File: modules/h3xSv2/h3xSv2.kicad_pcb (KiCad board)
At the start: 2 copper layers, 135.9 x 40.6 mm, 25 parts, among them J1 Conn_01x10_Male, J10 Conn_01x02_Male, J11 Conn_01x06_Male, J12 Conn_01x10_Male, J13 Conn_01x10_Male, J2 Conn_01x10_Male, J3 Conn_01x10_Male, J4 Conn_01x10_Male, J5 Conn_01x04_Male, J6 Conn_01x04_Male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

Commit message: New h3xSv2 is ready
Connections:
- J7 pad 12: VCC -> /13
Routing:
- net /A5: track 106.8 -> 161.7 mm, vias 1 -> 3
- net /3: track 102.6 -> 157.2 mm, vias 1 -> 3
- net /2: track 106.4 -> 160.7 mm, vias 1 -> 3
- net /A4: track 108.7 -> 162.7 mm, vias 1 -> 3
- net /4: track 97.5 -> 151.1 mm, vias 1 -> 3
- net /A3: track 65.9 -> 118.9 mm, vias 1 -> 3
- net /5: track 92.8 -> 145.5 mm, vias 1 -> 3
- net /A2: track 64.0 -> 116.0 mm, vias 1 -> 3
- net /6: track 88.2 -> 140.0 mm, vias 1 -> 3
- net /7: track 84.0 -> 134.8 mm, vias 1 -> 3
- net /A1: track 61.9 -> 112.6 mm, vias 1 -> 3
- net GND: track 168.3 -> 218.9 mm, vias 2 -> 4
- net /A0: track 60.2 -> 110.3 mm, vias 1 -> 3
- net /8: track 79.7 -> 129.6 mm, vias 1 -> 3
- net /13: track 75.1 -> 124.3 mm, vias 1 -> 3
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
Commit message: Add hash & gerber
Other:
- rule solder_mask_min_width: 0.25 -> 0.1
- board text added: "11.11.2020"
- board text added: "3f4a18"
- board text added: "v2"

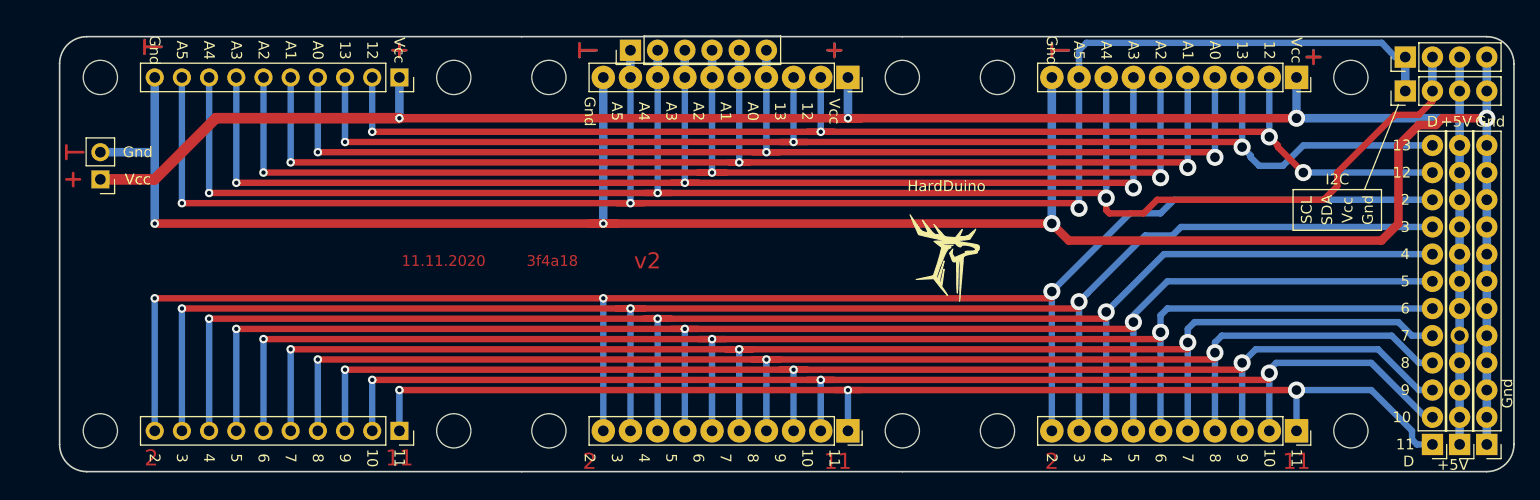
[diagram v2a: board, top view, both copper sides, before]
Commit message: Now 2x shields have distance between 1x parts
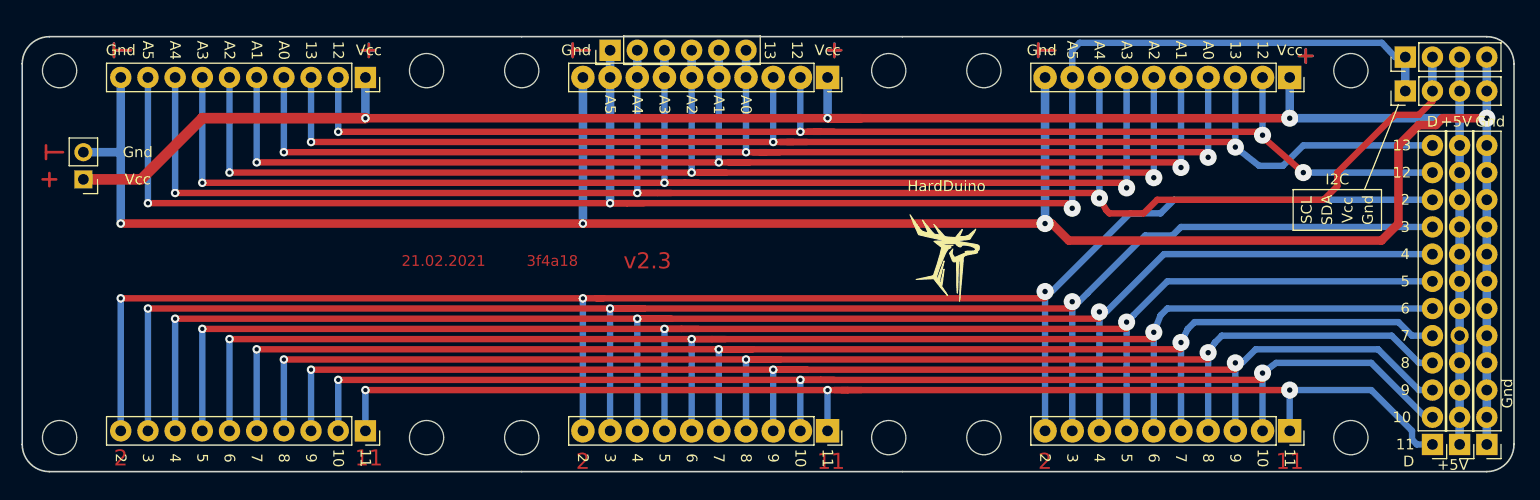
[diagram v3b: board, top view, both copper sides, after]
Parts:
- moved H9 3.86 mm to (36.8, 27.3)
- moved H12 3.86 mm to (36.8, 61.6)
- moved J12 3.17 mm to (65.4, 27.9)
- moved J13 3.17 mm to (65.4, 61.0)
- moved H11 2.62 mm to (71.1, 27.3)
- moved H3 2.62 mm to (80.0, 27.3)
- moved H1 2.62 mm to (80.0, 61.6)
- moved H10 2.62 mm to (71.1, 61.6)
- moved J1 1.91 mm to (108.6, 27.9)
- moved J11 1.91 mm to (88.3, 25.4)
- moved J2 1.91 mm to (108.6, 61.0)
- moved J10 1.59 mm to (39.1, 37.5)
- moved H4 1.42 mm to (114.3, 27.3)
- moved H6 1.42 mm to (123.2, 27.3)
- moved H2 1.42 mm to (114.3, 61.6)
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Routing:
- net /A5: track 161.7 -> 165.5 mm
- net /13: track 124.3 -> 127.9 mm
- net /12: track 118.8 -> 122.4 mm
- net /10: track 119.2 -> 122.8 mm
- net /5: track 145.5 -> 148.9 mm
- net /8: track 129.6 -> 133.0 mm
- net /A4: track 162.7 -> 166.0 mm
- net /7: track 134.8 -> 138.1 mm
- net /6: track 140.0 -> 143.3 mm
- net /A3: track 118.9 -> 122.1 mm
- net /A2: track 116.0 -> 119.2 mm
- net /A0: track 110.3 -> 113.5 mm
- net /9: track 124.0 -> 127.2 mm
- net /4: track 151.1 -> 154.3 mm
- net /A1: track 112.6 -> 115.7 mm
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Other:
- board size 135.9 x 40.6 mm -> 139.4 x 40.6 mm
- board text added: "21.02.2021"
- board text added: "v2.3"
- board text removed: "11.11.2020"
- board text removed: "v2"
